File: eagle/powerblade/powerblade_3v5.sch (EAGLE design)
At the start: 77 parts, among them J1 JTAG_14PIN_IDC-ND, J2 AC_INFINAL, J4 TC2030-JLINK-NL, Q1 NTS4173, Q4 2SK1829, U1 TPS62122, U2 MCP6V3, U3 MSP430FR5738, U4 NRF51822QF, U6 MAX9910, U7 OPA2369, X1 16MHz, X3 32.768kHz, Y1 UREACH_XTEND

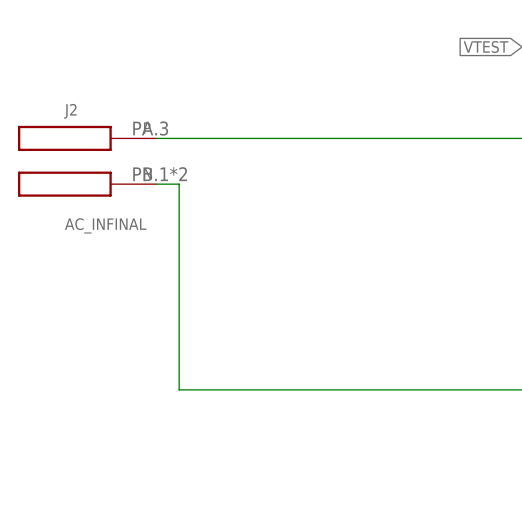
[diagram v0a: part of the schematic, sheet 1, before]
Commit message: updated powerblade to use new cutouts
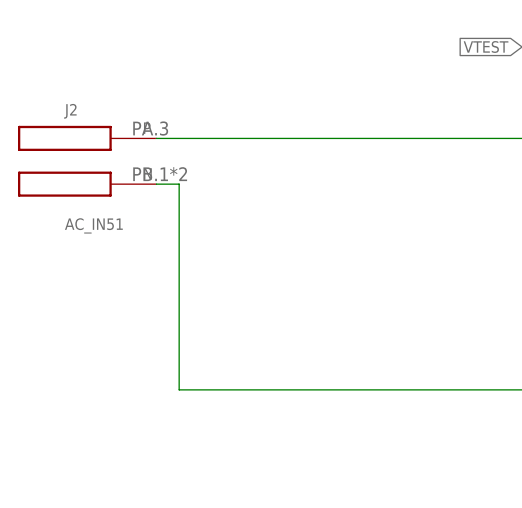
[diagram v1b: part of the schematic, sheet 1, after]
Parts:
- J2: value AC_INFINAL -> AC_IN51; device powerfilm:AC_INFINAL -> powerfilm:AC_IN51
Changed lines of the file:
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@@
 <grid distance="0.1" unitdist="inch" unit="inch" style="lines" multiple="1" display="no" altdistance="0.01" altunitdist="inch" altunit="inch"/>
 <layers>
-<layer number="1" name="Top" color="4" fill="1" visible="no" active="no"/>
-<layer number="2" name="Route2" color="1" fill="3" visible="no" active="no"/>
-<layer number="3" name="Route3" color="4" fill="3" visible="no" active="no"/>
-<layer number="4" name="Route4" color="1" fill="4" visible="no" active="no"/>
-<layer number="5" name="Route5" color="4" fill="4" visible="no" active="no"/>
-<layer number="6" name="Route6" color="1" fill="8" visible="no" active="no"/>
-<layer number="7" name="Route7" color="4" fill="8" visible="no" active="no"/>
-<layer number="8" name="Route8" color="1" fill="2" visible="no" active="no"/>
-<layer number="9" name="Route9" color="4" fill="2" visible="no" active="no"/>
-<layer number="10" name="Route10" color="1" fill="7" visible="no" active="no"/>
-<layer number="11" name="Route11" color="4" fill="7" visible="no" active="no"/>
-<layer number="12" name="Route12" color="1" fill="5" visible="no" active="no"/>
-<layer number="13" name="Route13" color="4" fill="5" visible="no" active="no"/>
-<layer number="14" name="Route14" color="1" fill="6" visible="no" active="no"/>
-<layer number="15" name="Route15" color="4" fill="6" visible="no" active="no"/>
-<layer number="16" name="Bottom" color="1" fill="1" visible="no" active="no"/>
-<layer number="17" name="Pads" color="2" fill="1" visible="no" active="no"/>
-<layer number="18" name="Vias" color="2" fill="1" visible="no" active="no"/>
-<layer number="19" name="Unrouted" color="6" fill="1" visible="no" active="no"/>
-<layer number="20" name="Dimension" color="15" fill="1" visible="no" active="no"/>
-<layer number="21" name="tPlace" color="7" fill="1" visible="no" active="no"/>
-<layer number="22" name="bPlace" color="7" fill="1" visible="no" active="no"/>
-<layer number="23" name="tOrigins" color="15" fill="1" visible="no" active="no"/>
-<layer number="24" name="bOrigins" color="15" fill="1" visible="no" active="no"/>
-<layer number="25" name="tNames" color="7" fill="1" visible="no" active="no"/>
-<layer number="26" name="bNames" color="7" fill="1" visible="no" active="no"/>
-<layer number="27" name="tValues" color="7" fill="1" visible="no" active="no"/>
-<layer number="28" name="bValues" color="7" fill="1" visible="no" active="no"/>
+<layer number="1" name="Top" color="4" fill="1" visible="yes" active="no"/>
+<layer number="2" name="Route2" color="1" fill="3" visible="yes" active="no"/>
+<layer number="3" name="Route3" color="4" fill="3" visible="yes" active="no"/>
+<layer number="4" name="Route4" color="1" fill="4" visible="yes" active="no"/>
+<layer number="5" name="Route5" color="4" fill="4" visible="yes" active="no"/>
+<layer number="6" name="Route6" color="1" fill="8" visible="yes" active="no"/>
+<layer number="7" name="Route7" color="4" fill="8" visible="yes" active="no"/>
+<layer number="8" name="Route8" color="1" fill="2" visible="yes" active="no"/>
+<layer number="9" name="Route9" color="4" fill="2" visible="yes" active="no"/>
+<layer number="10" name="Route10" color="1" fill="7" visible="yes" active="no"/>
+<layer number="11" name="Route11" color="4" fill="7" visible="yes" active="no"/>
+<layer number="12" name="Route12" color="1" fill="5" visible="yes" active="no"/>
+<layer number="13" name="Route13" color="4" fill="5" visible="yes" active="no"/>
+<layer number="14" name="Route14" color="1" fill="6" visible="yes" active="no"/>
+<layer number="15" name="Route15" color="4" fill="6" visible="yes" active="no"/>
+<layer number="16" name="Bottom" color="1" fill="1" visible="yes" active="no"/>
+<layer number="17" name="Pads" color="2" fill="1" visible="yes" active="no"/>
+<layer number="18" name="Vias" color="2" fill="1" visible="yes" active="no"/>
+<layer number="19" name="Unrouted" color="6" fill="1" visible="yes" active="no"/>
+<layer number="20" name="Dimension" color="15" fill="1" visible="yes" active="no"/>
+<layer number="21" name="tPlace" color="7" fill="1" visible="yes" active="no"/>
+<layer number="22" name="bPlace" color="7" fill="1" visible="yes" active="no"/>
+<layer number="23" name="tOrigins" color="15" fill="1" visible="yes" active="no"/>
+<layer number="24" name="bOrigins" color="15" fill="1" visible="yes" active="no"/>
+<layer number="25" name="tNames" color="7" fill="1" visible="yes" active="no"/>
+<layer number="26" name="bNames" color="7" fill="1" visible="yes" active="no"/>
+<layer number="27" name="tValues" color="7" fill="1" visible="yes" active="no"/>
+<layer number="28" name="bValues" color="7" fill="1" visible="yes" active="no"/>
 <layer number="29" name="tStop" color="7" fill="3" visible="no" active="no"/>
 <layer number="30" name="bStop" color="7" fill="6" visible="no" active="no"/>
@@
 <layer number="35" name="tGlue" color="7" fill="4" visible="no" active="no"/>
 <layer number="36" name="bGlue" color="7" fill="5" visible="no" active="no"/>
-<layer number="37" name="tTest" color="7" fill="1" visible="no" active="no"/>
-<layer number="38" name="bTest" color="7" fill="1" visible="no" active="no"/>
+<layer number="37" name="tTest" color="7" fill="1" visible="yes" active="no"/>
+<layer number="38" name="bTest" color="7" fill="1" visible="yes" active="no"/>
 <layer number="39" name="tKeepout" color="4" fill="11" visible="no" active="no"/>
 <layer number="40" name="bKeepout" color="1" fill="11" visible="no" active="no"/>
@@
 <layer number="44" name="Drills" color="7" fill="1" visible="no" active="no"/>
 <layer number="45" name="Holes" color="7" fill="1" visible="no" active="no"/>
-<layer number="46" name="Milling" color="3" fill="1" visible="no" active="no"/>
-<layer number="47" name="Measures" color="7" fill="1" visible="no" active="no"/>
-<layer number="48" name="Document" color="7" fill="1" visible="no" active="no"/>
-<layer number="49" name="Reference" color="7" fill="1" visible="no" active="no"/>
-<layer number="50" name="dxf" color="7" fill="1" visible="no" active="no"/>
-<layer number="51" name="tDocu" color="7" fill="1" visible="no" active="no"/>
-<layer number="52" name="bDocu" color="7" fill="1" visible="no" active="no"/>
-<layer number="53" name="tGND_GNDA" color="7" fill="9" visible="no" active="no"/>
-<layer number="54" name="bGND_GNDA" color="1" fill="9" visible="no" active="no"/>
-<layer number="56" name="wert" color="7" fill="1" visible="no" active="no"/>
-<layer number="57" name="tCAD" color="7" fill="1" visible="no" active="no"/>
+<layer number="46" name="Milling" color="3" fill="1" visible="yes" active="no"/>
+<layer number="47" name="Measures" color="7" fill="1" visible="yes" active="no"/>
+<layer number="48" name="Document" color="7" fill="1" visible="yes" active="no"/>
+<layer number="49" name="Reference" color="7" fill="1" visible="yes" active="no"/>
+<layer number="50" name="dxf" color="7" fill="1" visible="yes" active="no"/>
+<layer number="51" name="tDocu" color="7" fill="1" visible="yes" active="no"/>
+<layer number="52" name="bDocu" color="7" fill="1" visible="yes" active="no"/>
+<layer number="53" name="tGND_GNDA" color="7" fill="9" visible="yes" active="no"/>
+<layer number="54" name="bGND_GNDA" color="1" fill="9" visible="yes" active="no"/>
+<layer number="56" name="wert" color="7" fill="1" visible="yes" active="no"/>
+<layer number="57" name="tCAD" color="7" fill="1" visible="yes" active="no"/>
 <layer number="91" name="Nets" color="2" fill="1" visible="yes" active="yes"/>
 <layer number="92" name="Busses" color="1" fill="1" visible="yes" active="yes"/>
@@
 <attribute name="DIGIKEY" value="490-4025-1-ND"/>
 </part>
-<part name="J2" library="powerfilm" deviceset="AC_IN" device="FINAL" value="AC_INFINAL">
+<part name="J2" library="powerfilm" deviceset="AC_IN" device="51" value="AC_IN51">
 <attribute name="DIGIKEY" value="ED1649-ND"/>
 <attribute name="DIGIKEY_2" value="ED1649-ND"/>
